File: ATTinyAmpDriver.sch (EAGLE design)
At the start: 24 parts, among them Q1 SI2301CDS, T1 BC846, U1 SPX5205M5-L-3-3, U2 ATTINY5-TSHR, U3 MCP6001, X1 DIODES, X2 INPUT

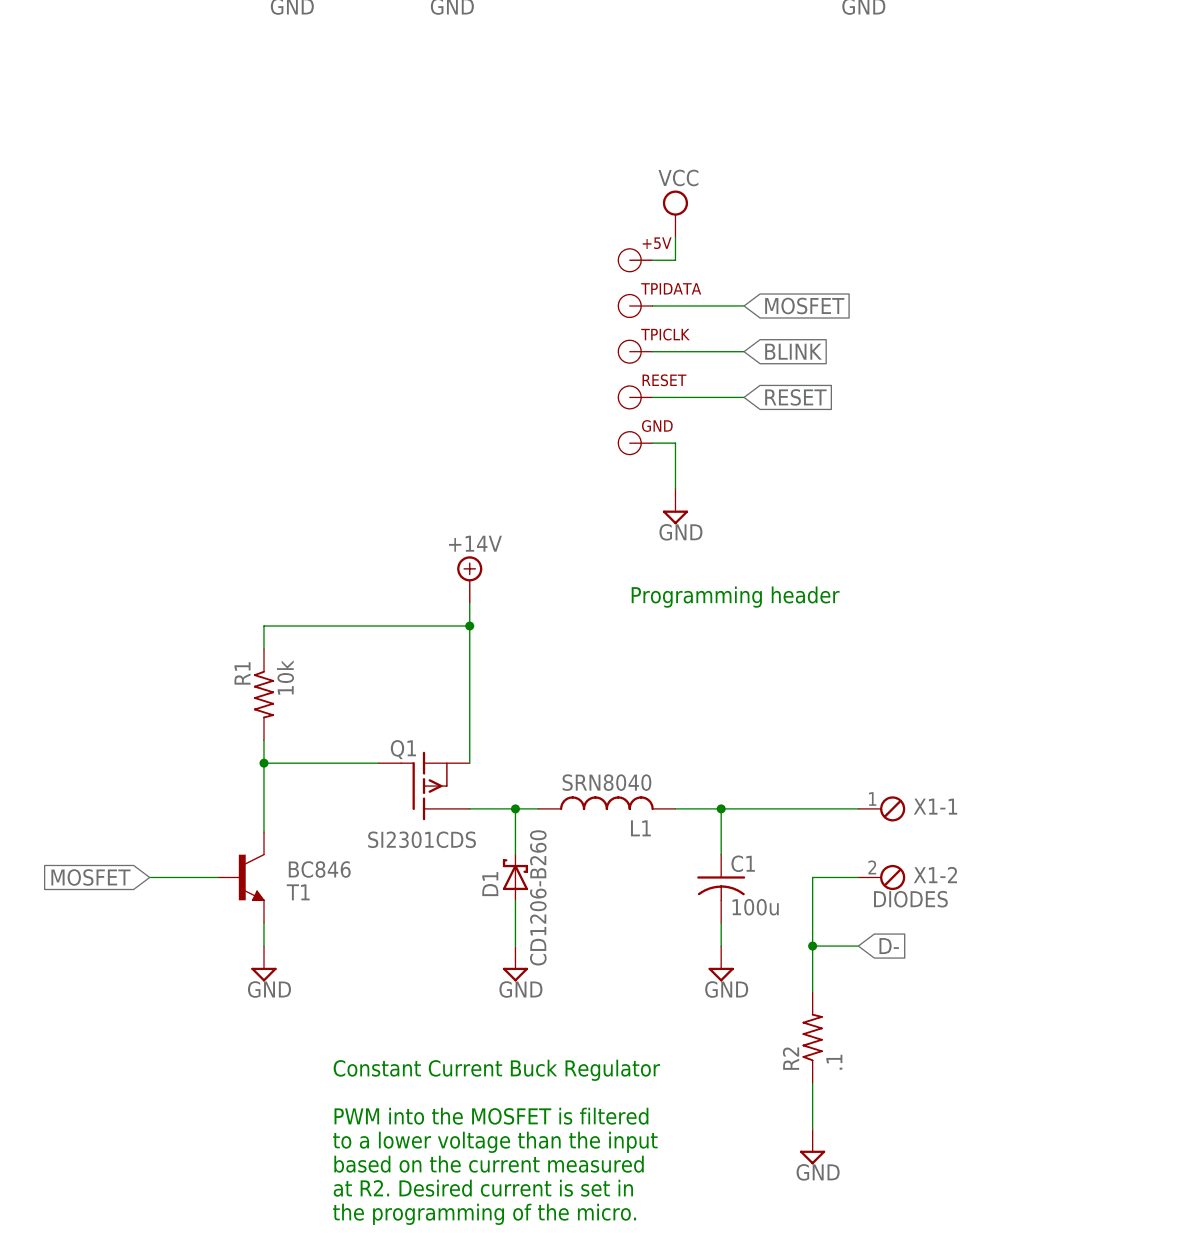
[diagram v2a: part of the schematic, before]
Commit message: Removed LED filter circuit
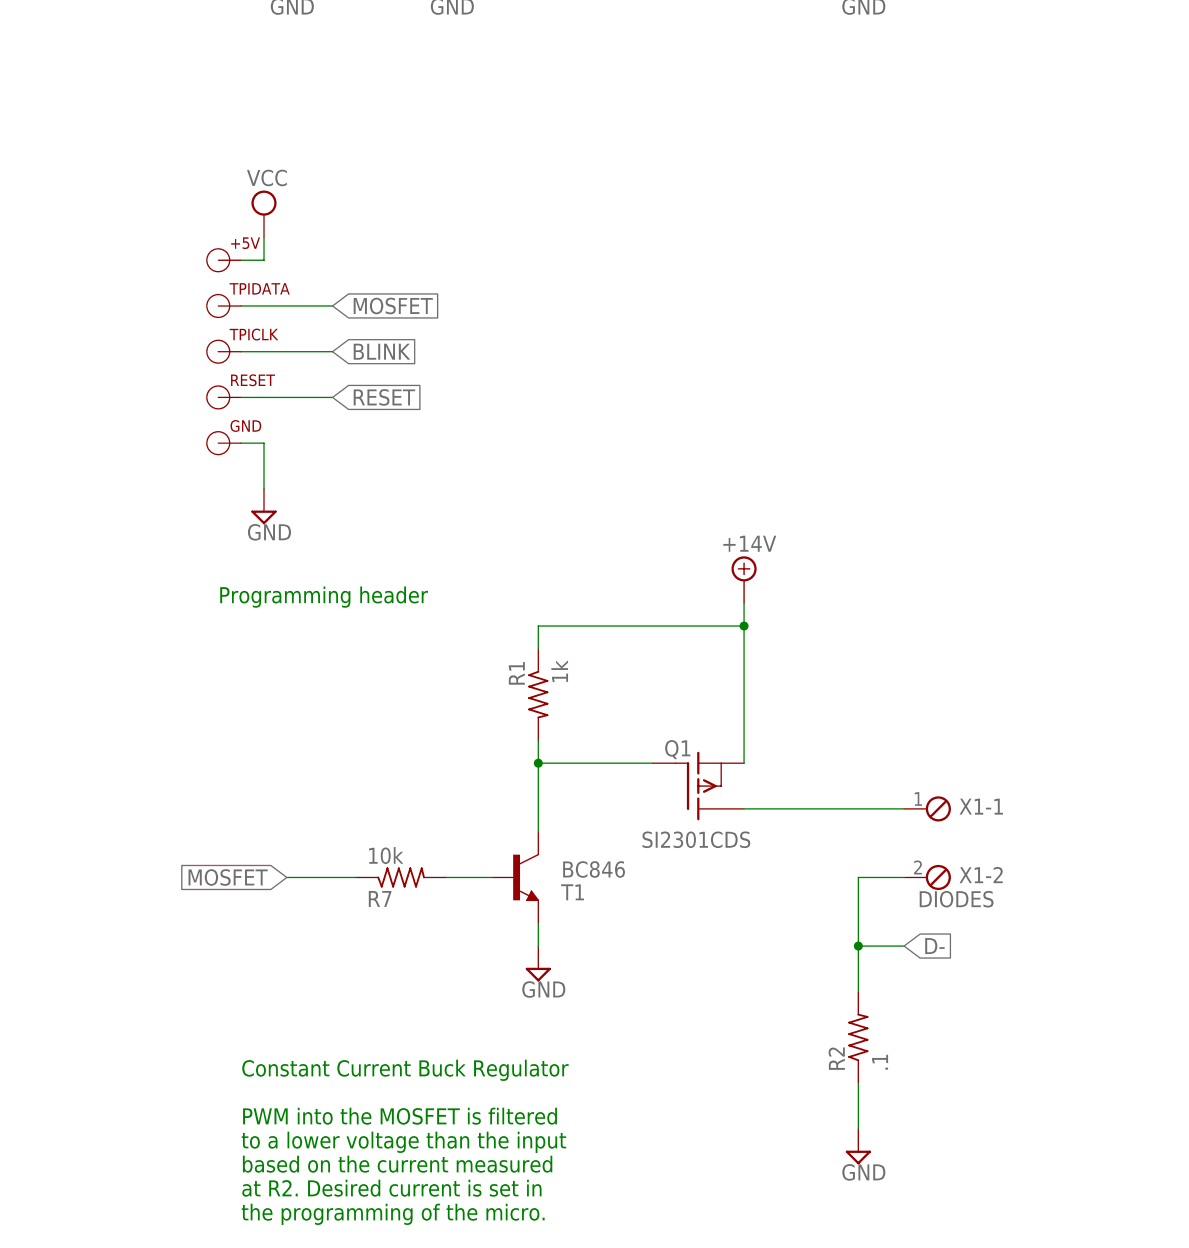
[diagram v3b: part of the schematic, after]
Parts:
- removed C1: 100u, Personal:AVE107M25X16T-F
- removed D1: CD1206-B260, Personal:CD1206-B260
- removed L1: SRN8040, Personal:SRN8040
- added R7: 10k, resistor:R-US_R1206
- R1: value 10k -> 1k
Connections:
- removed net L+: D1.C, L1.1, Q1.D
- new net N$6: R7.2, T1.B
- net GND: no longer C1.C-, D1.A
- net MOSFET: now also R7.1; no longer T1.B
- net N$3: now also Q1.D; no longer C1.C+, L1.2
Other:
- moved on the sheet: +5V, GND, Q1, R1, R2, RESET, T1, TPICLK, TPIDATA, X1-1, X1-2

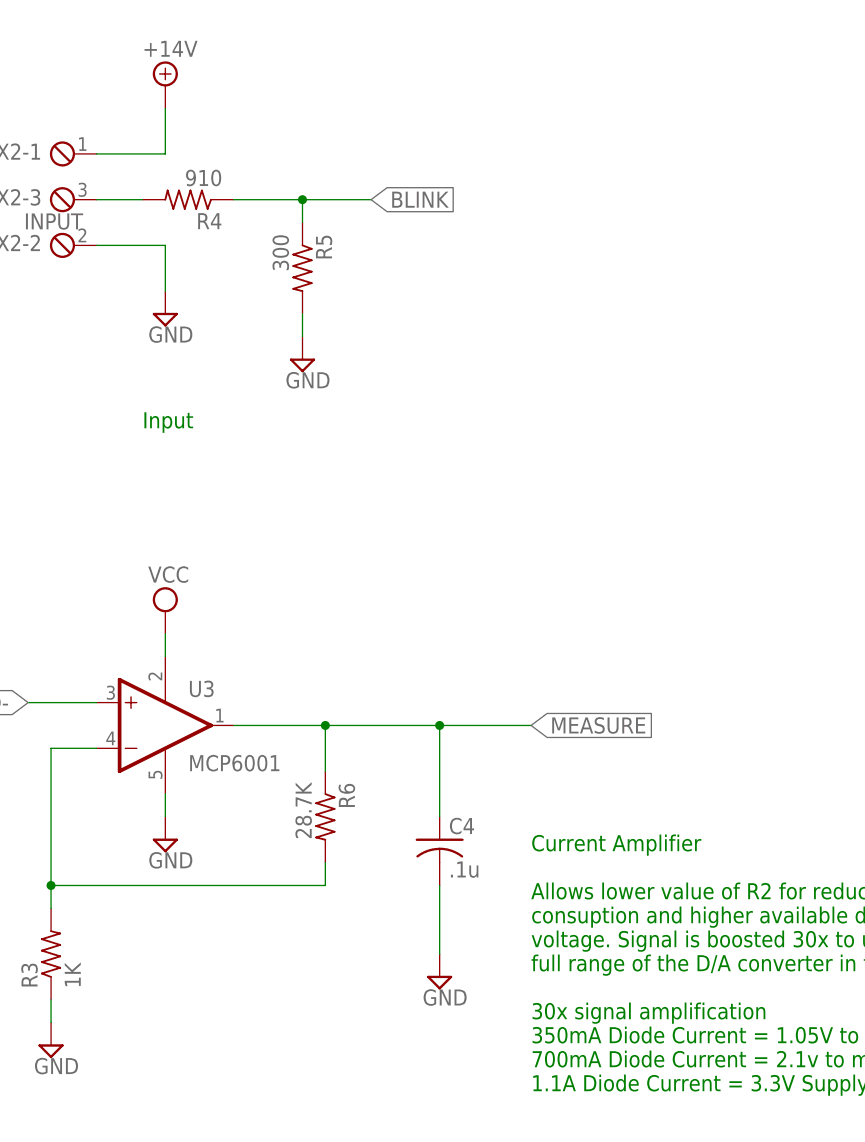
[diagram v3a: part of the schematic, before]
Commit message: Removed Cap from OpAmp Output
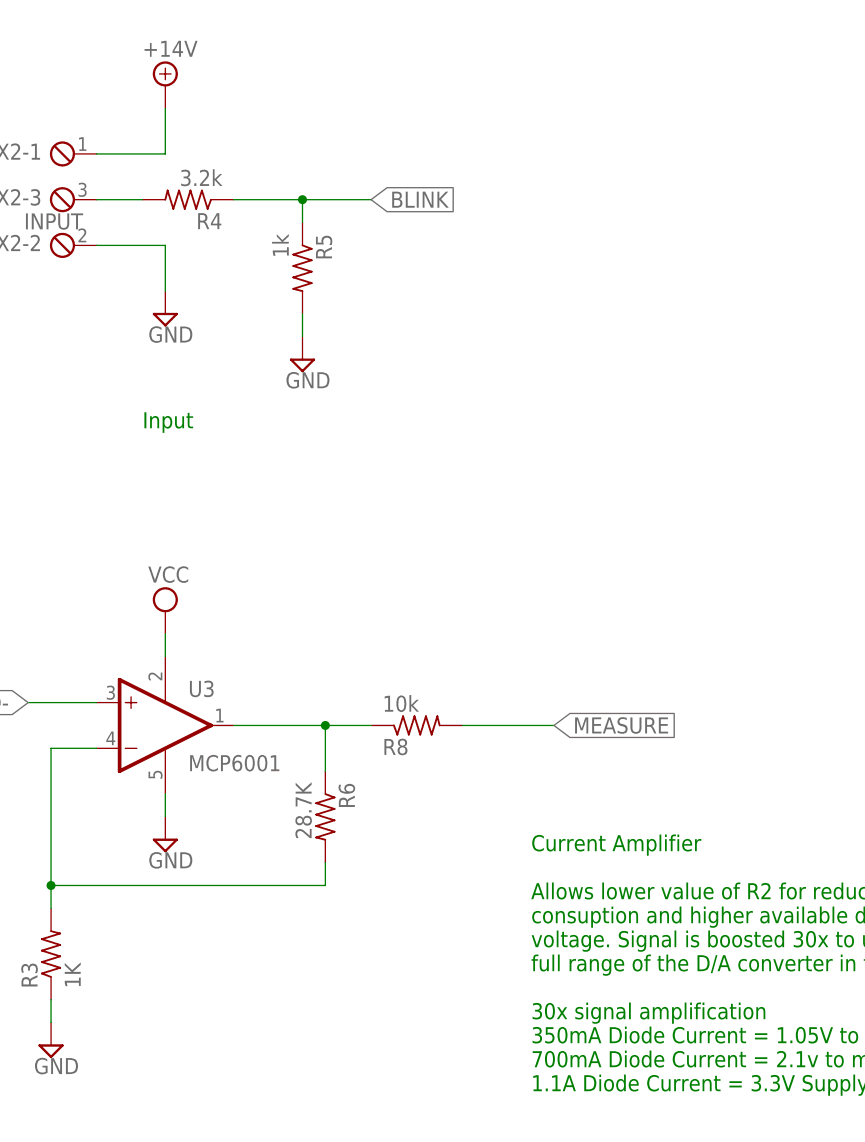
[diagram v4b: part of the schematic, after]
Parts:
- removed C4: .1u, resistor:C-USC0805
- added R8: 10k, resistor:R-US_R1206
- R4: value 910 -> 3.2k
- R5: value 300 -> 1k
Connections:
- new net OPAMP_OUT: R6.1, R8.1, U3.OUT
- net GND: no longer C4.2
- net MEASURE: now also R8.2; no longer C4.1, R6.1, U3.OUT
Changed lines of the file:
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@@
 </part>
 <part name="SUPPLY9" library="supply2" deviceset="+14V" device=""/>
-<part name="R4" library="resistor" deviceset="R-US_" device="R1206" value="910">
+<part name="R4" library="resistor" deviceset="R-US_" device="R1206" value="3.2k">
 <attribute name="DIGIKEY" value="RMCF1206JT910RCT-ND"/>
 <attribute name="DIGIKEY_COST" value=".05"/>
 </part>
-<part name="R5" library="resistor" deviceset="R-US_" device="R1206" value="300">
+<part name="R5" library="resistor" deviceset="R-US_" device="R1206" value="1k">
 <attribute name="DIGIKEY" value="RMCF1206JT300RCT-ND"/>
 <attribute name="DIGIKEY_COST" value=".05"/>
@@
 <part name="T1" library="transistor-neu-to92" deviceset="BC846" device=""/>
 <part name="SUPPLY14" library="supply2" deviceset="GND" device=""/>
-<part name="C4" library="resistor" deviceset="C-US" device="C0805" value=".1u">
-<attribute name="DIGIKEY" value="445-7534-1-ND"/>
-<attribute name="DIGIKEY_COST" value=".10"/>
-</part>
-<part name="SUPPLY18" library="supply2" deviceset="GND" device=""/>
 <part name="R7" library="resistor" deviceset="R-US_" device="R1206" value="10k">
+<attribute name="DIGIKEY" value="RMCF1206JT10K0CT-ND"/>
+<attribute name="DIGIKEY_COST" value=".05"/>
+</part>
+<part name="R8" library="resistor" deviceset="R-US_" device="R1206" value="10k">
 <attribute name="DIGIKEY" value="RMCF1206JT10K0CT-ND"/>
 <attribute name="DIGIKEY_COST" value=".05"/>
@@
 </instance>
 <instance part="SUPPLY14" gate="GND" x="78.74" y="50.8"/>
-<instance part="C4" gate="G$1" x="210.82" y="53.34">
-<attribute name="DIGIKEY" x="210.82" y="53.34" size="1.778" layer="96" display="off"/>
-<attribute name="DIGIKEY_COST" x="210.82" y="53.34" size="1.778" layer="96" display="off"/>
-</instance>
-<instance part="SUPPLY18" gate="GND" x="210.82" y="38.1"/>
 <instance part="R7" gate="G$1" x="63.5" y="60.96" rot="MR180">
 <attribute name="DIGIKEY" x="63.5" y="60.96" size="1.778" layer="96" rot="MR180" display="off"/>
 <attribute name="DIGIKEY_COST" x="63.5" y="60.96" size="1.778" layer="96" rot="MR180" display="off"/>
+</instance>
+<instance part="R8" gate="G$1" x="208.28" y="66.04" rot="MR180">
+<attribute name="DIGIKEY" x="208.28" y="66.04" size="1.778" layer="96" rot="MR180" display="off"/>
+<attribute name="DIGIKEY_COST" x="208.28" y="66.04" size="1.778" layer="96" rot="MR180" display="off"/>
 </instance>
 </instances>
@@
 <pinref part="SUPPLY14" gate="GND" pin="GND"/>
 <wire x1="78.74" y1="55.88" x2="78.74" y2="53.34" width="0.1524" layer="91"/>
-</segment>
-<segment>
-<pinref part="C4" gate="G$1" pin="2"/>
-<pinref part="SUPPLY18" gate="GND" pin="GND"/>
-<wire x1="210.82" y1="48.26" x2="210.82" y2="40.64" width="0.1524" layer="91"/>
 </segment>
 </net>
@@
 <net name="MEASURE" class="0">
 <segment>
-<wire x1="187.96" y1="66.04" x2="198.12" y2="66.04" width="0.1524" layer="91"/>
-<label x="220.98" y="66.04" size="1.778" layer="95" rot="MR180" xref="yes"/>
-<pinref part="U3" gate="G$1" pin="OUT"/>
-<pinref part="R6" gate="G$1" pin="1"/>
-<wire x1="198.12" y1="66.04" x2="210.82" y2="66.04" width="0.1524" layer="91"/>
-<wire x1="210.82" y1="66.04" x2="220.98" y2="66.04" width="0.1524" layer="91"/>
-<wire x1="198.12" y1="60.96" x2="198.12" y2="66.04" width="0.1524" layer="91"/>
-<junction x="198.12" y="66.04"/>
-<pinref part="C4" gate="G$1" pin="1"/>
-<wire x1="210.82" y1="55.88" x2="210.82" y2="66.04" width="0.1524" layer="91"/>
-<junction x="210.82" y="66.04"/>
-</segment>
-<segment>
 <wire x1="205.74" y1="177.8" x2="218.44" y2="177.8" width="0.1524" layer="91"/>
 <label x="218.44" y="177.8" size="1.778" layer="95" xref="yes"/>
 <pinref part="U2" gate="A" pin="PB2"/>
+</segment>
+<segment>
+<pinref part="R8" gate="G$1" pin="2"/>
+<wire x1="213.36" y1="66.04" x2="223.52" y2="66.04" width="0.1524" layer="91"/>
+<label x="223.52" y="66.04" size="1.778" layer="95" xref="yes"/>
 </segment>
 </net>
@@
 </segment>
 </net>
+<net name="OPAMP_OUT" class="0">
+<segment>
+<wire x1="187.96" y1="66.04" x2="198.12" y2="66.04" width="0.1524" layer="91"/>
+<pinref part="U3" gate="G$1" pin="OUT"/>
+<pinref part="R6" gate="G$1" pin="1"/>
+<wire x1="198.12" y1="60.96" x2="198.12" y2="66.04" width="0.1524" layer="91"/>
+<pinref part="R8" gate="G$1" pin="1"/>
+<wire x1="203.2" y1="66.04" x2="198.12" y2="66.04" width="0.1524" layer="91"/>
+<junction x="198.12" y="66.04"/>
+</segment>
+</net>
